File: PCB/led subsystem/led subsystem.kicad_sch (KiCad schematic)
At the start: 3 parts, among them U1 MCU_Seeed_XIAO_ESP32-C3

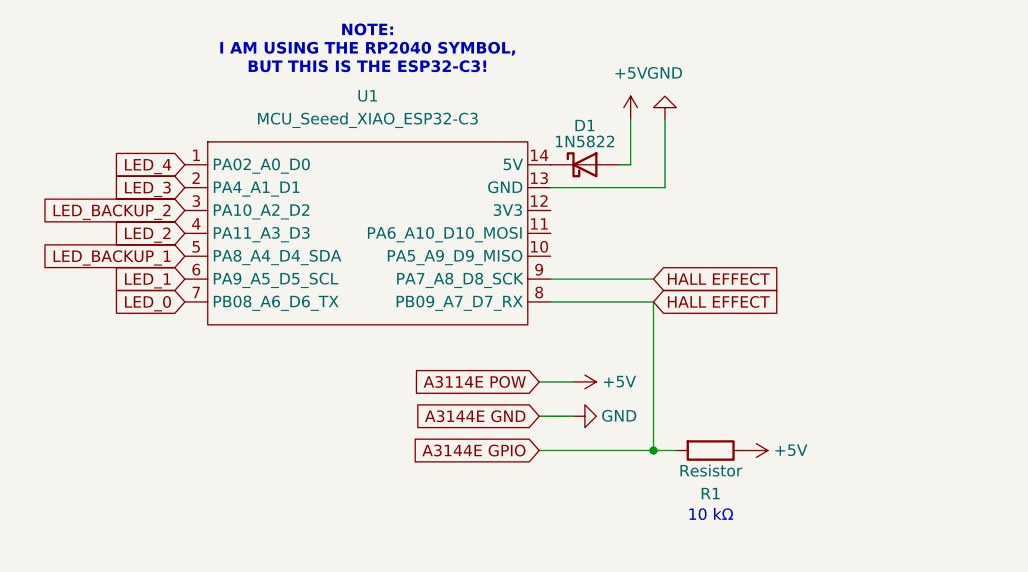
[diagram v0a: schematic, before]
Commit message: updated LED panel ground fill pour
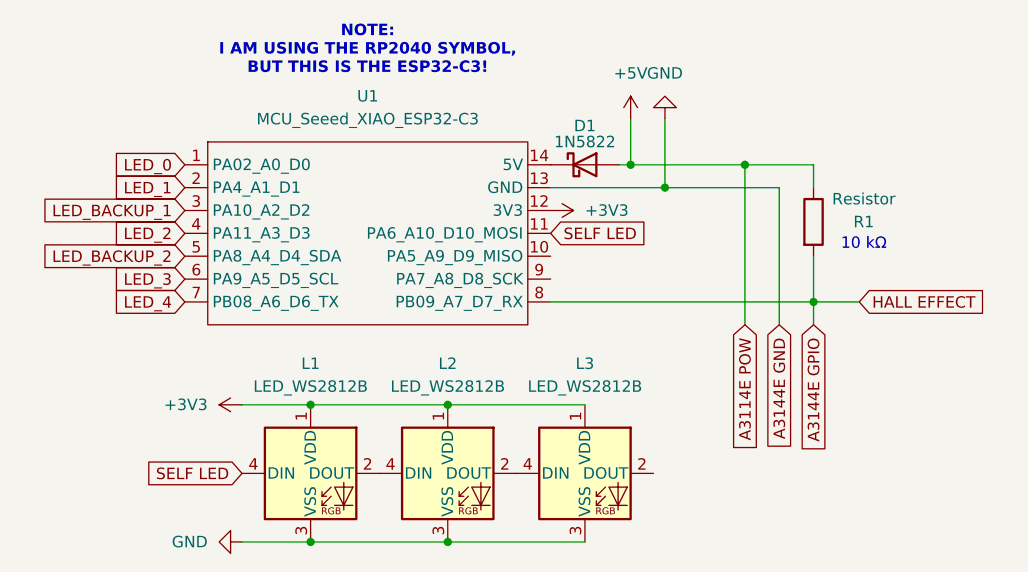
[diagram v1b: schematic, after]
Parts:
- added L1, L2, L3: LED_WS2812B, ScottoKeebs_Components:LED_WS2812B, symbol ScottoKeebs:LED_WS2812B
- U1: footprint (none) -> ScottoKeebs_MCU:Seeed_XIAO_RP2040
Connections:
- net A3144E GPIO: no longer U1.9 (PA7_A8_D8_SCK)
- net GND: now also L1.3 (VSS), L2.3 (VSS), L3.3 (VSS)
- net LED_0: now also U1.1 (PA02_A0_D0); no longer U1.7 (PB08_A6_D6_TX)
- net LED_1: now also U1.2 (PA4_A1_D1); no longer U1.6 (PA9_A5_D5_SCL)
- net LED_3: now also U1.6 (PA9_A5_D5_SCL); no longer U1.2 (PA4_A1_D1)
- net LED_4: now also U1.7 (PB08_A6_D6_TX); no longer U1.1 (PA02_A0_D0)
- net LED_BACKUP_1: now also U1.3 (PA10_A2_D2); no longer U1.5 (PA8_A4_D4_SDA)
- net LED_BACKUP_2: now also U1.5 (PA8_A4_D4_SDA); no longer U1.3 (PA10_A2_D2)
- net SELF LED: now reaches U1.11 (PA6_A10_D10_MOSI)
- net SELF LED: now also L1.4 (DIN)
- net +3V3: now reaches U1.12 (3V3)
- net +3V3: now also L1.1 (VDD), L2.1 (VDD), L3.1 (VDD)
- new net: L2.2 (DOUT), L3.4 (DIN)
- new net: L1.2 (DOUT), L2.4 (DIN)
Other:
- moved on the sheet: R1

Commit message: 07122025 - firmware plans and two PCBs in one day!
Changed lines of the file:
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@@
-	(wire
-		(pts
-			(xy 144.78 77.47) (xy 149.86 77.47)
-		)
-		(stroke
-			(width 0)
-			(type default)
-		)
-	)
 	(wire
 		(pts
@@
 				(hide yes)
 			)
-		)
-	)
-	(global_label "HALL EFFECT"
-		(shape input)
-		(at 149.86 77.47 0)
-		(fields_autoplaced yes)
-		(effects
-			(font
-				(size 1.27 1.27)
-			)
-			(justify left)
-		)
-		(property "Intersheetrefs" "${INTERSHEET_REFS}"
-			(at 165.0009 77.47 0)
-			(effects
-				(font
-					(size 1.27 1.27)
-				)
-				(justify left)
-				(hide yes)
-			)

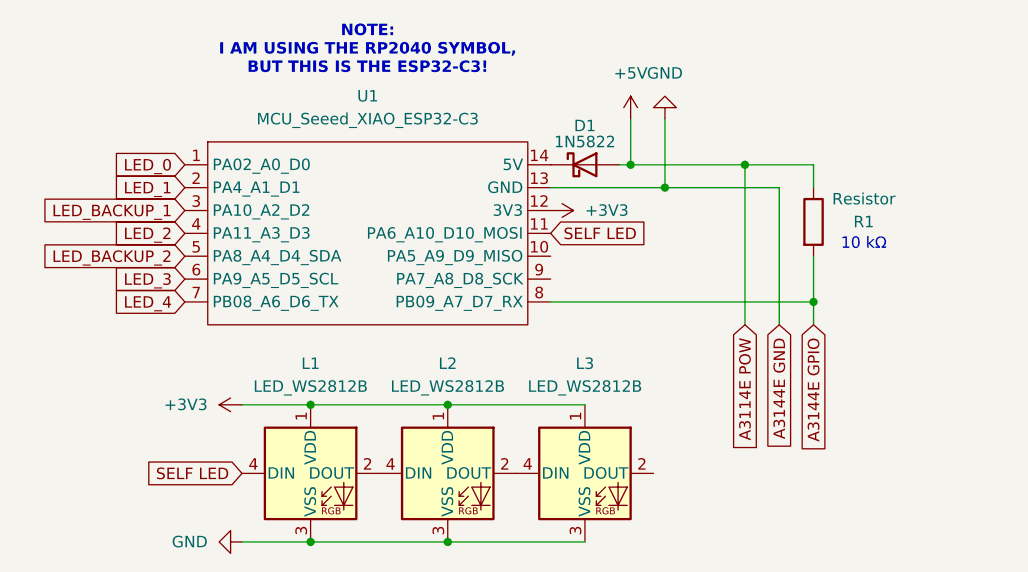
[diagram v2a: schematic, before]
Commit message: 07242025 - parts and almost finishing BOM!
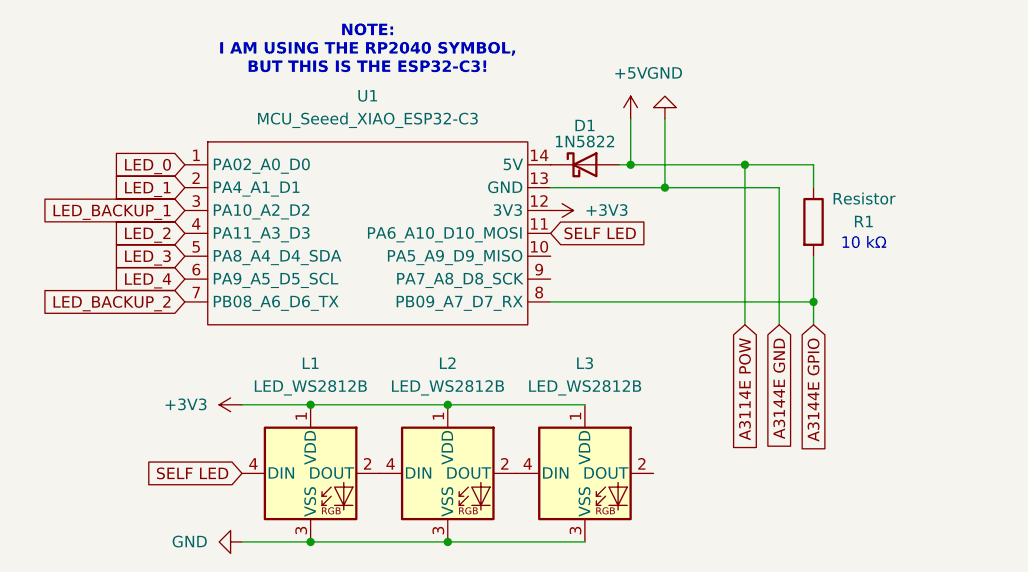
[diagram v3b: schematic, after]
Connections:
- net LED_3: now also U1.5 (PA8_A4_D4_SDA); no longer U1.6 (PA9_A5_D5_SCL)
- net LED_4: now also U1.6 (PA9_A5_D5_SCL); no longer U1.7 (PB08_A6_D6_TX)
- net LED_BACKUP_2: now also U1.7 (PB08_A6_D6_TX); no longer U1.5 (PA8_A4_D4_SDA)
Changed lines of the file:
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@@
 	(global_label "LED_4"
 		(shape input)
-		(at 74.93 77.47 180)
+		(at 74.93 74.93 180)
 		(fields_autoplaced yes)
 		(effects
@@
 		)
 		(property "Intersheetrefs" "${INTERSHEET_REFS}"
-			(at 66.3206 77.47 0)
+			(at 66.3206 74.93 0)
 			(effects
 				(font
@@
 	(global_label "LED_BACKUP_2"
 		(shape input)
-		(at 74.93 72.39 180)
+		(at 74.93 77.47 180)
 		(fields_autoplaced yes)
 		(effects
@@
 		)
 		(property "Intersheetrefs" "${INTERSHEET_REFS}"
-			(at 57.8539 72.39 0)
+			(at 57.8539 77.47 0)
 			(effects
 				(font
@@
 	(global_label "LED_3"
 		(shape input)
-		(at 74.93 74.93 180)
+		(at 74.93 72.39 180)
 		(fields_autoplaced yes)
 		(effects
@@
 		)
 		(property "Intersheetrefs" "${INTERSHEET_REFS}"
-			(at 66.3206 74.93 0)
+			(at 66.3206 72.39 0)
 			(effects
 				(font
